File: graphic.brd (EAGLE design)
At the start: 109 x 29.5 mm, 73 parts, among them IC1 NE5532D, IC2 NE5532D, IC3 NE5532D, IC4 NE5532D, IC5 NE5532D

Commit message: Prototype 1 sent to OSHPark
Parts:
- added C31, C32, C33, C34, C35, C36, C37, C38: NP, we-rcl:C0805
- added U$1: (no value), MusicThingModular:TMKF
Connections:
- new net N$22: IC5.1, IC5.2
- net GND: now also IC5.3
- net N$11: now also C34.1, C35.2
- net N$12: now also C33.2
- net N$14: now also C31.1
- net N$18: now also C31.2
- net N$19: now also C36.1
- net N$23: now also C37.1, C38.1
- net N$30: now also C32.1
- net N$31: now also C33.1
- net N$36: now also C34.2, C35.1
- net N$37: now also C36.2
- net N$4: now also C32.2
- net N$40: now also C37.2, C38.2
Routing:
- net N$11: track 6.96 -> 18.9 mm
- net N$23: track 7.59 -> 18.0 mm
- net N$19: track 10.0 -> 18.5 mm
- net N$12: track 9.63 -> 18.1 mm
- net N$4: track 10.3 -> 18.8 mm
- net -12V: track 94.1 -> 101.4 mm
- net N$18: track 5.72 -> 12.2 mm
- net N$14: track 9.75 -> 15.8 mm
- net +12V: track 97.6 -> 103.2 mm
- net N$36: track 4.60 -> 9.20 mm
- net N$40: track 3.81 -> 7.62 mm
- net N$31: track 5.72 -> 7.63 mm
- net N$30: track 6.50 -> 8.41 mm
- net N$37: track 7.62 -> 9.53 mm
- net +_INLET: track 104.6 -> 105.9 mm
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
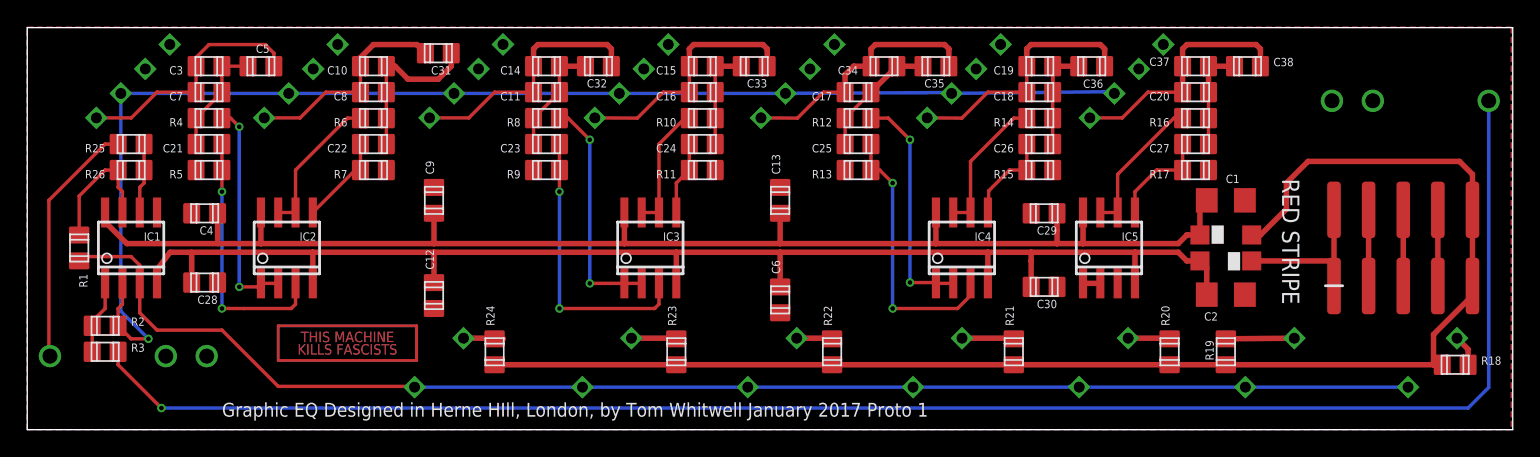
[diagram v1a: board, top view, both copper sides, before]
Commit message: updated 20mm fader outlines - NOT moved yet
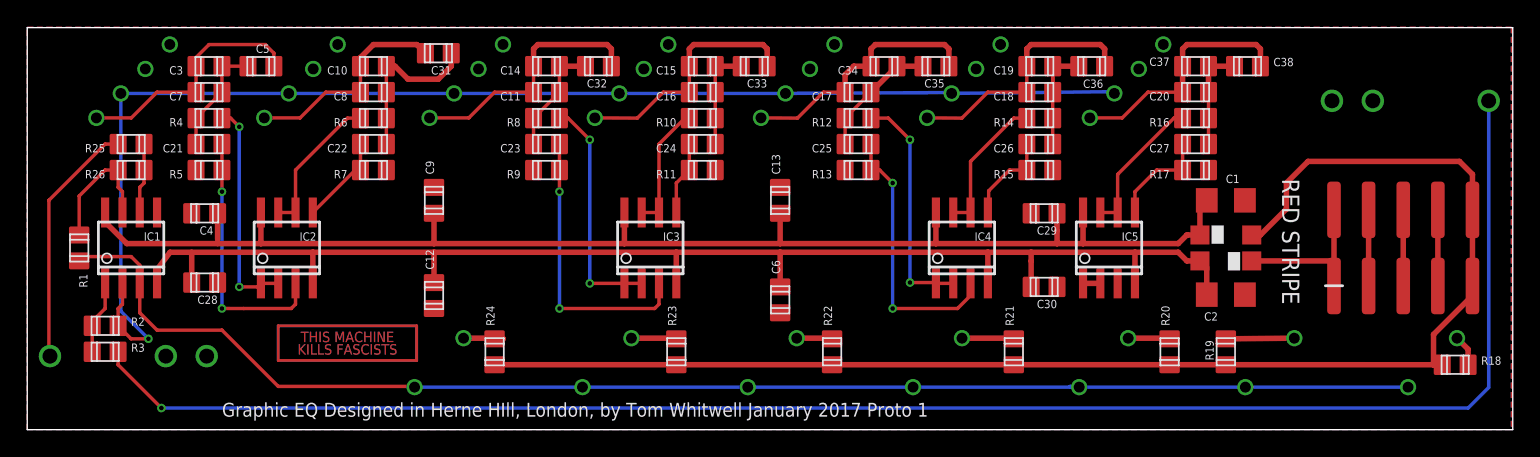
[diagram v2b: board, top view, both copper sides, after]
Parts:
- 160HZ, 16KHZ, 1KHZ, 2.5KHZ, 410HZ, 63HZ, 7.7KHZ: device TomW:ALPHA_ILL_FADER_20MM -> MusicThingModular:ALPHA_ILL_FADER_20MM_REV2

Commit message: move sliders and reverse movement
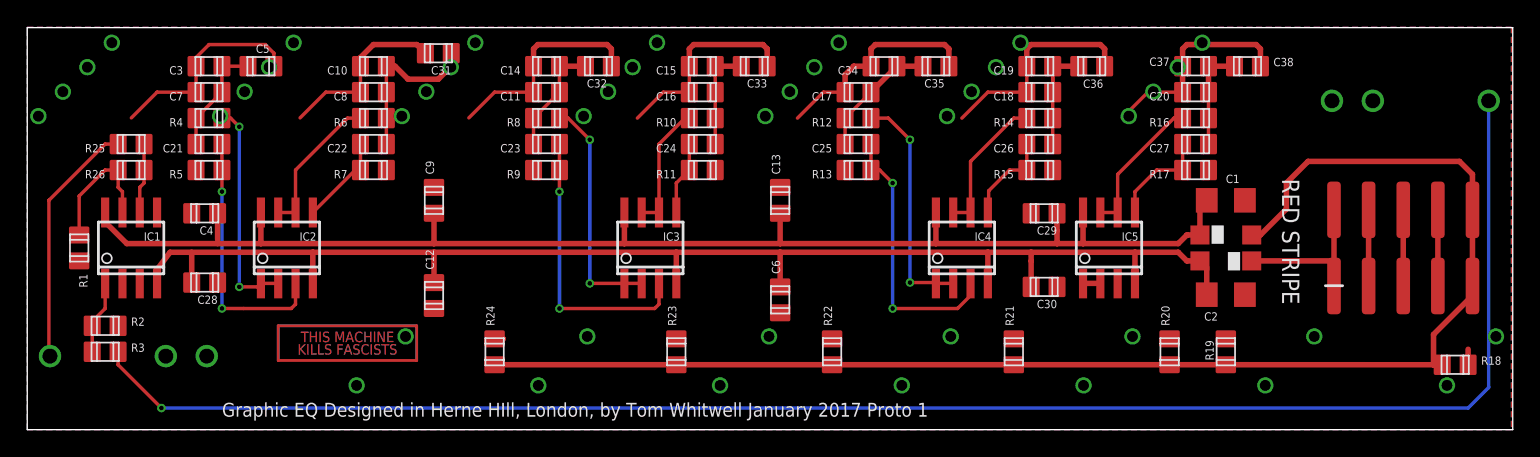
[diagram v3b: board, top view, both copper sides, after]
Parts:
- moved 63HZ 4.26 mm to (14.3, 14.9)
- moved 160HZ 3.24 mm to (27.6, 14.9)
- moved 16KHZ 2.86 mm to (94.3, 14.9)
- moved 410HZ 2.04 mm to (41.0, 14.9)
- moved 7.7KHZ 1.47 mm to (81.0, 14.9)
- moved 1KHZ 0.84 mm to (54.3, 14.9)
- moved 2.5KHZ 0.34 mm to (67.6, 14.9)
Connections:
- net N$3: now also IC1.2, R2.1; no longer IC1.3, R1.1
- net N$7: now also IC1.3, R1.1; no longer IC1.2, R2.1
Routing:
- net N$3: track 105.0 -> 0.00 mm
- net N$7: track 97.7 -> 0.00 mm, vias 1 -> 0
- net N$13: track 5.04 -> 0.00 mm
- net N$20: track 3.82 -> 0.07 mm
- net N$42: track 3.31 -> 0.07 mm
- net N$12: track 18.1 -> 15.0 mm
- net N$15: track 3.06 -> 0.07 mm
- net N$4: track 18.8 -> 16.0 mm
- net N$43: track 3.57 -> 0.70 mm
- net N$11: track 18.9 -> 16.2 mm
- net N$14: track 15.8 -> 13.2 mm
- net N$8: track 18.0 -> 15.4 mm
- net N$19: track 18.5 -> 16.0 mm
- net N$41: track 2.62 -> 0.07 mm
- net N$23: track 18.0 -> 15.6 mm
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
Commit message: re route and redesign panel
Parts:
- moved C37 3.81 mm to (89.5, 26.7)
- moved C38 3.81 mm to (93.3, 26.7)
- moved C21 3.81 mm to (9.53, 21.0)
- moved C3 3.81 mm to (9.53, 26.7)
- moved C7 3.81 mm to (9.53, 24.8)
- moved R4 3.81 mm to (9.53, 22.9)
- moved R5 3.81 mm to (9.53, 19.1)
- moved C5 3.81 mm to (13.3, 26.7)
- moved C19 1.91 mm to (76.2, 26.7)
- moved C20 1.91 mm to (87.6, 24.8)
- moved C31 1.91 mm to (28.3, 27.6)
- moved C36 1.91 mm to (80.0, 26.7)
- moved U$1 1.91 mm to (21.6, 6.35)
- moved R25 1.91 mm to (5.71, 21.0)
- moved R26 1.91 mm to (5.71, 19.1)
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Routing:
- net N$7: track 0.00 -> 103.3 mm, vias 0 -> 1
- net N$3: track 0.00 -> 102.4 mm
- net N$42: track 0.07 -> 6.67 mm
- net N$43: track 0.70 -> 7.31 mm
- net N$13: track 0.00 -> 6.56 mm
- net N$4: track 16.0 -> 20.8 mm
- net N$41: track 0.07 -> 4.77 mm
- net N$20: track 0.07 -> 4.77 mm
- net N$14: track 13.2 -> 17.1 mm
- net N$12: track 15.0 -> 18.9 mm
- net N$25: track 19.1 -> 22.9 mm
- net N$8: track 15.4 -> 18.4 mm
- net N$15: track 0.07 -> 2.86 mm
- net N$26: track 16.2 -> 18.9 mm
- net N$10: track 1.14 -> 3.57 mm
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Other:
- board text added: "Graphic EQ Designed in Herne HIll, London, by Tom Whitwell February 2017 Proto 2"
- board text removed: "Graphic EQ Designed in Herne HIll, London, by Tom Whitwell January 2017 Proto 1"

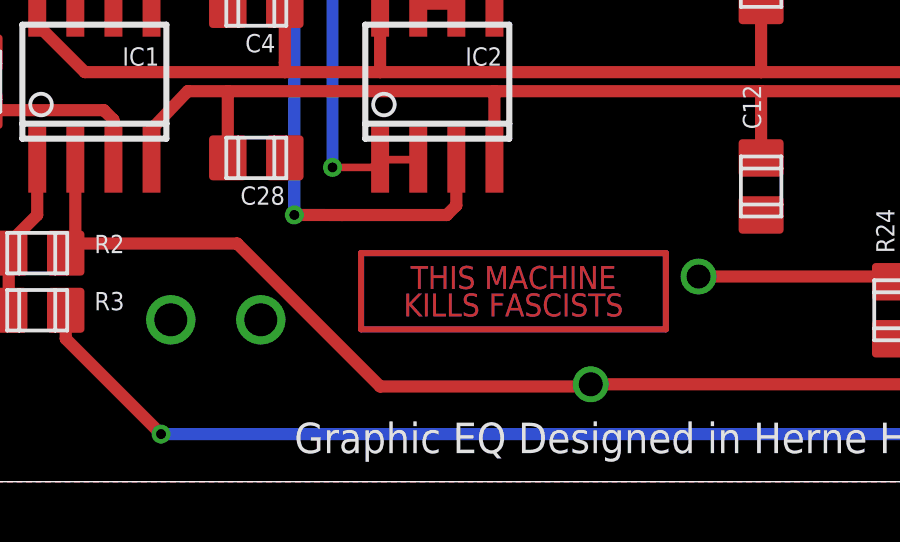
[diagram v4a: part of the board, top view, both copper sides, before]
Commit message: Updated illuminated fader outline
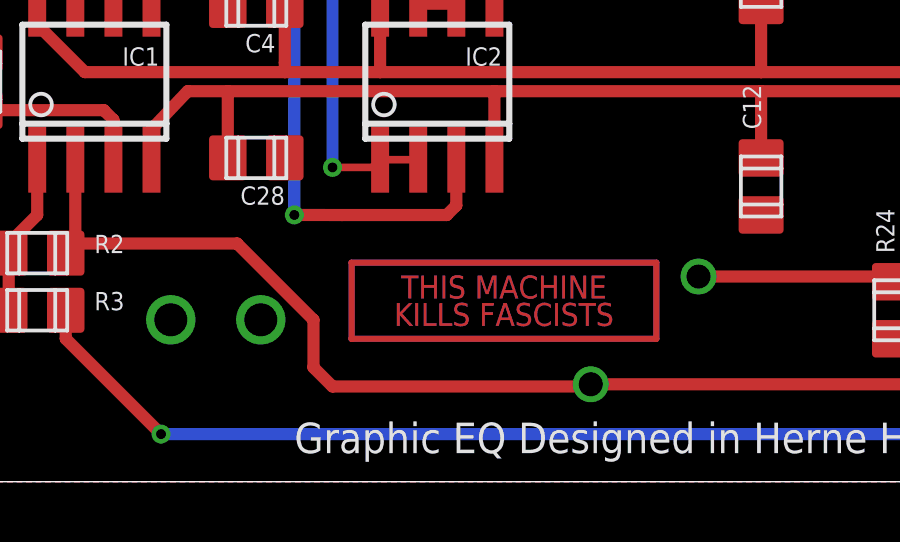
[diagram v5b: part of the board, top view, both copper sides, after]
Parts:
- moved U$1 0.45 mm to (21.3, 6.03)
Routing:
- net N$3: track 102.4 -> 103.4 mm
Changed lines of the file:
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@@
 <layer number="50" name="dxf" color="7" fill="1" visible="no" active="no"/>
 <layer number="51" name="tDocu" color="7" fill="1" visible="no" active="yes"/>
-<layer number="52" name="bDocu" color="7" fill="1" visible="no" active="yes"/>
+<layer number="52" name="bDocu" color="7" fill="1" visible="yes" active="yes"/>
 <layer number="53" name="tGND_GNDA" color="7" fill="9" visible="no" active="no"/>
 <layer number="54" name="bGND_GNDA" color="1" fill="9" visible="no" active="no"/>
@@
 </element>
 <element name="C38" library="we-rcl" package="C0805" value="NP" x="93.345" y="26.67" rot="R270"/>
-<element name="U$1" library="MusicThingModular" package="TMKF" value="" x="21.59" y="6.35"/>
+<element name="U$1" library="MusicThingModular" package="TMKF" value="" x="21.2725" y="6.0325"/>
 </elements>
 <signals>
@@
 <wire x1="6.985" y1="7.94" x2="6.665" y2="7.62" width="0.254" layer="1"/>
 <wire x1="6.985" y1="7.94" x2="12.38" y2="7.94" width="0.4064" layer="1"/>
-<wire x1="12.38" y1="7.94" x2="17.145" y2="3.175" width="0.4064" layer="1"/>
-<wire x1="17.145" y1="3.175" x2="24.09261875" y2="3.175" width="0.4064" layer="1"/>
+<wire x1="12.38" y1="7.94" x2="14.9225" y2="5.3975" width="0.4064" layer="1"/>
+<wire x1="14.9225" y1="5.3975" x2="14.9225" y2="3.81" width="0.4064" layer="1"/>
+<wire x1="14.9225" y1="3.81" x2="15.5575" y2="3.175" width="0.4064" layer="1"/>
+<wire x1="15.5575" y1="3.175" x2="24.09261875" y2="3.175" width="0.4064" layer="1"/>
 <wire x1="24.09261875" y1="3.175" x2="24.165784375" y2="3.248165625" width="0.254" layer="1"/>
 <wire x1="24.165784375" y1="3.248165625" x2="37.500784375" y2="3.248165625" width="0.4064" layer="1"/>

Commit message: Increase LED resistors to reduce current draw
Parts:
- R18, R19, R20, R21, R22, R23, R24: value 470R -> 2k
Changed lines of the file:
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@@
 <?xml version="1.0" encoding="utf-8"?>
 <!DOCTYPE eagle SYSTEM "eagle.dtd">
-<eagle version="7.4.0">
+<eagle version="7.2.0">
 <drawing>
 <settings>
@@
 <element name="R16" library="we-rcl" package="C0805" value="1.8k" x="85.725" y="22.86" rot="R90"/>
 <element name="R17" library="we-rcl" package="C0805" value="51k" x="85.725" y="19.05" rot="R90"/>
-<element name="R18" library="we-rcl" package="C0805" value="470R" x="104.775" y="4.7625" rot="R270"/>
-<element name="R19" library="we-rcl" package="C0805" value="470R" x="87.9475" y="5.715" smashed="yes">
+<element name="R18" library="we-rcl" package="C0805" value="2k" x="104.775" y="4.7625" rot="R270"/>
+<element name="R19" library="we-rcl" package="C0805" value="2k" x="87.9475" y="5.715" smashed="yes">
 <attribute name="NAME" x="87.0585" y="5.08" size="0.6096" layer="25" font="vector" ratio="10" rot="R270" align="top-right"/>
 <attribute name="VALUE" x="89.5985" y="4.699" size="0.6096" layer="27" font="vector" ratio="10" rot="R270" align="top-right"/>
 </element>
-<element name="R20" library="we-rcl" package="C0805" value="470R" x="83.82" y="5.715"/>
-<element name="R21" library="we-rcl" package="C0805" value="470R" x="72.39" y="5.715"/>
-<element name="R22" library="we-rcl" package="C0805" value="470R" x="59.055" y="5.715"/>
-<element name="R23" library="we-rcl" package="C0805" value="470R" x="47.625" y="5.715"/>
-<element name="R24" library="we-rcl" package="C0805" value="470R" x="34.29" y="5.715"/>
+<element name="R20" library="we-rcl" package="C0805" value="2k" x="83.82" y="5.715"/>
+<element name="R21" library="we-rcl" package="C0805" value="2k" x="72.39" y="5.715"/>
+<element name="R22" library="we-rcl" package="C0805" value="2k" x="59.055" y="5.715"/>
+<element name="R23" library="we-rcl" package="C0805" value="2k" x="47.625" y="5.715"/>
+<element name="R24" library="we-rcl" package="C0805" value="2k" x="34.29" y="5.715"/>
 <element name="R25" library="we-rcl" package="C0805" value="10k" x="5.715" y="20.955" rot="R90"/>
 <element name="R26" library="we-rcl" package="C0805" value="10k" x="5.715" y="19.05" rot="R90"/>

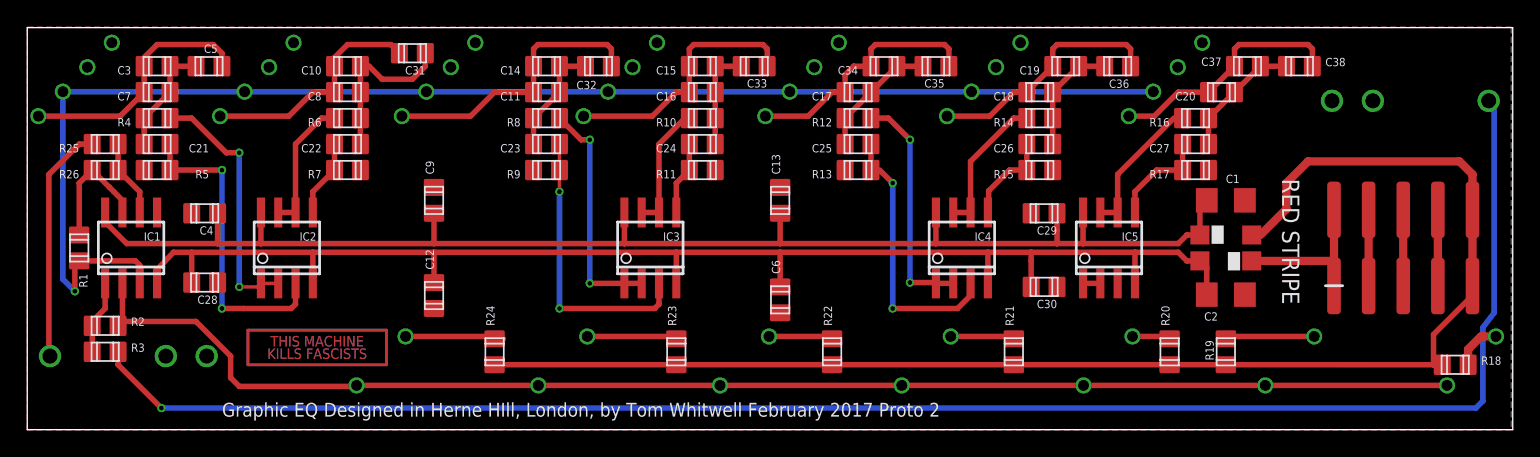
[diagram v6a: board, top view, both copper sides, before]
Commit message: Tweaks for Rev 1 boards: improve ground plane clearance, move one resistor, move Kills Fascists arwork, small changes to get ground plane to work
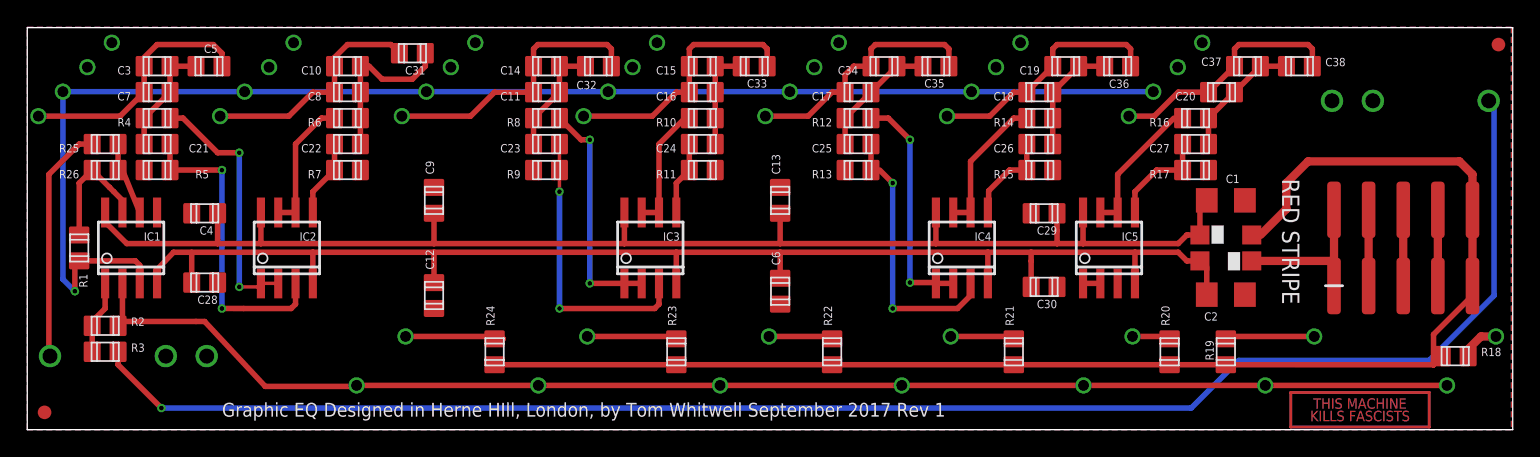
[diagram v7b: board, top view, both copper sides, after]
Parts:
- added FID1, FID2: FIDUCIAL1X2.5, SparkFun-Aesthetics:FIDUCIAL-1X2.5
- moved U$1 76.7 mm to (97.8, 1.46)
- moved C6 0.63 mm to (55.2, 10.2)
- moved R18 0.63 mm to (104.8, 5.40)
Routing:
- net N$6: track 125.1 -> 121.1 mm
- net N$3: track 103.4 -> 102.5 mm
- net -12V: track 101.0 -> 100.4 mm
- net N$10: track 3.57 -> 2.93 mm
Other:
- board text added: "Graphic EQ Designed in Herne HIll, London, by Tom Whitwell September 2017 Rev 1"
- board text removed: "Graphic EQ Designed in Herne HIll, London, by Tom Whitwell February 2017 Proto 2"
